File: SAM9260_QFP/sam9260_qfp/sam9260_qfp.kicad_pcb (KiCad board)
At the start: 4 copper layers, 164 parts, among them J101 Conn_ARM_JTAG_SWD_10, J201 USB_B_Micro, J202 Micro_SD_Card, J203 RJ45, J301 USB_A, J302 USB_A, SW101 SW_Push, SW102 SW_DIP_x01, U101 AT91SAM9260-QU, U201 USBLC6-2SC6, U202 LD1117S33TR_SOT223, U203 RTL8211EG-VB-CG, U301 USBLC6-2SC6, U302 USB2514B_Bi, U303 MIC2099-1YMT-TR, U304 MIC2099-1YMT-TR, U305 USBLC6-2SC6, U306 USBLC6-2SC6, Y101 18MHz, Y201 25Mhz, Y301 24MHz

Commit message: Completed component placing
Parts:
- added C135: 4.7u, Capacitor_SMD:C_0603_1608Metric, F.Cu at (128.0, 82.0)
- added C235: 100n, Capacitor_SMD:C_0402_1005Metric, F.Cu at (95.7, 57.8)
- added FB101: 120R, Inductor_SMD:L_0603_1608Metric, F.Cu at (127.2, 84.5)
- FB201, FB301, FB302, FB303: footprint Inductor_SMD:L_0805_2012Metric -> Inductor_SMD:L_0603_1608Metric
- U101: footprint My_First_PCB:PQFP208_ATM -> SAM9260:PQFP208_ATM
- U303, U304: footprint My_First_PCB:TMLF-6_MT_MCH -> MIC2099:TMLF-6_MT_MCH
- XMER201: footprint My_First_PCB:H5007NL_PUL -> H5007NL:H5007NL_PUL
- moved C319 231.2 mm to (85.8, 167.8), turned to 180 degrees
- moved C321 222.7 mm to (86.3, 169.5), turned to 180 degrees
- moved J302 221.9 mm to (86.8, 175.3)
- moved D301 215.0 mm to (91.3, 153.0)
- moved U305 211.5 mm to (107.1, 164.0), turned to -90 degrees
- moved C318 210.5 mm to (105.8, 167.8), turned to 180 degrees
- moved C315 208.9 mm to (90.3, 137.7), turned to -90 degrees
- moved C323 207.8 mm to (86.3, 171.0), turned to 180 degrees
- moved R309 207.2 mm to (93.8, 150.8), turned to -90 degrees
- moved C312 207.0 mm to (92.0, 132.7), turned to 180 degrees
- moved C309 206.5 mm to (88.8, 137.7), turned to -90 degrees
- moved C224 206.1 mm to (66.3, 56.0)
- moved C305 203.2 mm to (89.5, 129.7), turned to 180 degrees
- moved C222 203.1 mm to (66.3, 57.5)
- moved C219 203.0 mm to (66.3, 60.5)
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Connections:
- C112 pad 1: +3.3V -> +3.3VA
- C113 pad 1: +3.3V -> +3.3VA
- C220 pad 1: Net-(C220-Pad1) -> AVDD10
- C223 pad 1: Net-(C220-Pad1) -> AVDD10
- C227 pad 1: Net-(C220-Pad1) -> AVDD10
- C229 pad 1: Net-(C229-Pad1) -> AVDD10
- C230 pad 1: Net-(C229-Pad1) -> AVDD10
- C231 pad 1: Net-(C229-Pad1) -> AVDD10
- J101 pad 1: AVDD10 -> +3.3V
- U101 pad 160: +3.3V -> +3.3VA

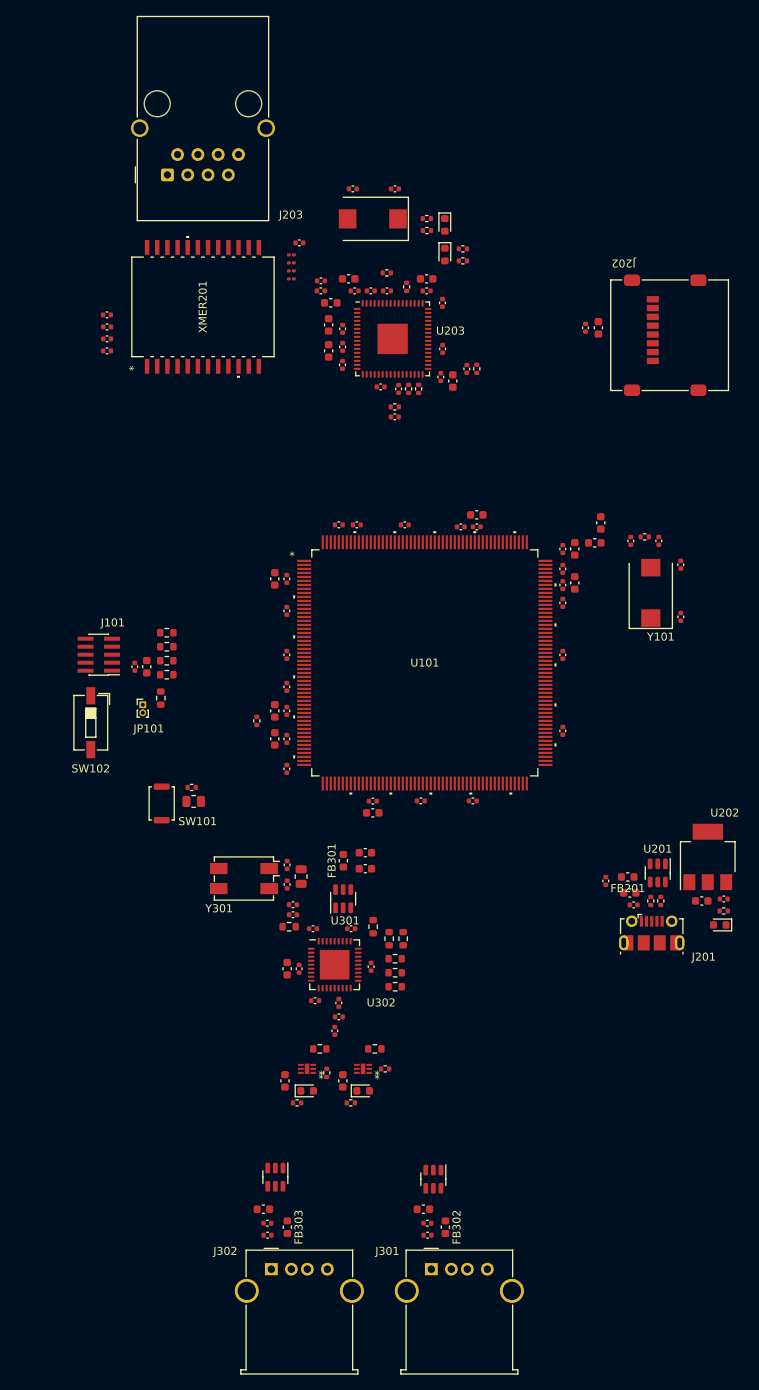
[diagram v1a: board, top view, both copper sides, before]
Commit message: updated layout
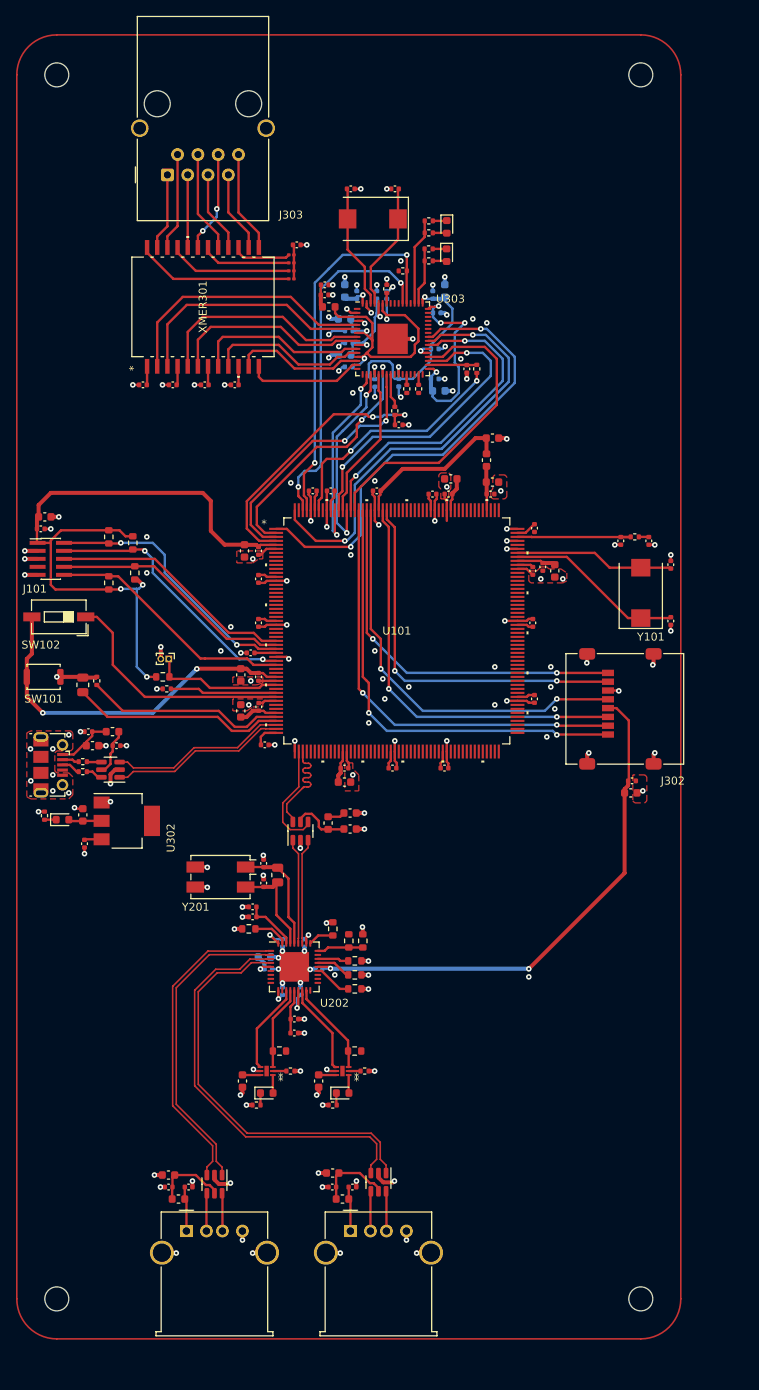
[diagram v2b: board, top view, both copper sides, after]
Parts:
- removed the C132 at (112.5, 81.0)
- removed the C135 at (128.0, 82.0)
- removed the R108 at (73.8, 97.5)
- removed the R109 at (73.8, 99.2)
- added C103: 10u, Capacitor_SMD:C_0603_1608Metric, F.Cu at (96.0, 114.4)
- added C111: 100n, Capacitor_SMD:C_0402_1005Metric, F.Cu at (119.5, 88.0)
- added H201: MountingHole, MountingHole:MountingHole_3mm, F.Cu at (133.0, 179.0)
- added H202: MountingHole, MountingHole:MountingHole_3mm, F.Cu at (60.0, 179.0)
- added H203: MountingHole, MountingHole:MountingHole_3mm, F.Cu at (60.0, 26.0)
- added H204: MountingHole, MountingHole:MountingHole_3mm, F.Cu at (133.0, 26.0)
- added R104: 1k, Resistor_SMD:R_0402_1005Metric, F.Cu at (65.0, 101.8)
- added R105: 100k, Resistor_SMD:R_0603_1608Metric, F.Cu at (69.8, 88.2)
- C102, C121, C123, C131: value 100n -> 10u; footprint Capacitor_SMD:C_0402_1005Metric -> Capacitor_SMD:C_0603_1608Metric
- C104, C110, C114, C122: value 10u -> 100n; footprint Capacitor_SMD:C_0603_1608Metric -> Capacitor_SMD:C_0402_1005Metric
- C113: value 4.7u -> 100n; footprint Capacitor_SMD:C_0603_1608Metric -> Capacitor_SMD:C_0402_1005Metric
- C120, C125: value 100n -> 4.7u; footprint Capacitor_SMD:C_0402_1005Metric -> Capacitor_SMD:C_0603_1608Metric
- C209: renamed from C309; moved to B.Cu
- C210: renamed from C310; moved to B.Cu
- C211: renamed from C311; moved to B.Cu
- C212: renamed from C312; moved to B.Cu
- C213: renamed from C313; moved to B.Cu
- C214: renamed from C314; moved to B.Cu
- C215: renamed from C315; moved to B.Cu
- C308: renamed from C208; moved to B.Cu
- C309: renamed from C209; moved to B.Cu
- C310: renamed from C210; moved to B.Cu
- C311: renamed from C211; moved to B.Cu
- C312: renamed from C212; moved to B.Cu
- C313: renamed from C213; moved to B.Cu
- C314: renamed from C214; moved to B.Cu
- C315: renamed from C215; moved to B.Cu
- C316: renamed from C216; moved to B.Cu
- C317: renamed from C217; moved to B.Cu
- C318: renamed from C220; moved to B.Cu
- C321: renamed from C223; moved to B.Cu
- C324: renamed from C227; moved to B.Cu
- C328: renamed from C235; moved to B.Cu
- C330: renamed from C229; moved to B.Cu
- C331: renamed from C230; moved to B.Cu
- C332: renamed from C231; moved to B.Cu
- R101: value 1.5M -> 1k; footprint Resistor_SMD:R_0805_2012Metric -> Resistor_SMD:R_0402_1005Metric
- R102: value 1k -> 1.5M; footprint Resistor_SMD:R_0402_1005Metric -> Resistor_SMD:R_0805_2012Metric
- R103: value 1k -> 100k; footprint Resistor_SMD:R_0402_1005Metric -> Resistor_SMD:R_0603_1608Metric
- U101: value AT91SAM9260-QU -> AT91SAM9260B-QU
- XMER301: renamed from XMER201; footprint H5007NL:H5007NL_PUL -> HL5007:H5007NL_PUL
- moved R303 85.7 mm to (58.5, 118.6), turned to -90 degrees
- moved D301 83.2 mm to (60.7, 119.1), turned to 0 degrees
- moved C304 80.2 mm to (63.5, 122.1), turned to -90 degrees
- moved C307 78.1 mm to (63.2, 118.5), turned to 90 degrees
- moved J301 78.0 mm to (59.2, 112.2), turned to -90 degrees
- moved R301 74.0 mm to (63.2, 113.1), turned to 0 degrees
- moved R302 73.1 mm to (63.2, 111.8), turned to 0 degrees
- moved U302 72.8 mm to (68.8, 119.2), turned to 0 degrees
- moved C302 71.5 mm to (63.9, 108.1)
- moved C301 69.6 mm to (64.5, 109.8), turned to 0 degrees
- moved U301 69.6 mm to (66.7, 112.8), turned to 180 degrees
- moved FB301 66.9 mm to (67.0, 108.1), turned to 0 degrees
- moved C128 66.8 mm to (58.5, 81.2), turned to 180 degrees
- moved C129 65.6 mm to (58.0, 82.8), turned to 180 degrees
- moved C303 63.5 mm to (67.5, 109.8), turned to 0 degrees
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- renumbered C103 to C132, C111 to C133, C133 to C134, C134 to C135, C301 to C201, C302 to C202, C303 to C203, C304 to C204, C305 to C205, C306 to C206, C307 to C207, C308 to C208, C316 to C216, C317 to C217, C318 to C218, C319 to C219, C320 to C220, C321 to C221, C322 to C222, C323 to C223, C201 to C301, C202 to C302, C203 to C303, C204 to C304, C205 to C305, C206 to C306, C207 to C307, C218 to C319, C219 to C320, C221 to C322, C222 to C323, C224 to C325, C225 to C326, C226 to C327, C228 to C329, C232 to C333, C233 to C334, C234 to C335, D301 to D201, D302 to D202, D201 to D301, D202 to D302, D203 to D303, FB301 to FB201, FB302 to FB202, FB303 to FB203, FB201 to FB301, J301 to J201, J302 to J202, J201 to J301, J202 to J302, J203 to J303, L201 to L301, R104 to R108, R105 to R109, R301 to R201, R302 to R202, R303 to R203, R304 to R204, R305 to R205, R306 to R206, R307 to R207, R308 to R208, R309 to R209, R310 to R210, R311 to R211, R312 to R212, R313 to R213, R314 to R214, R201 to R301, R202 to R302, R203 to R303, R204 to R304, R205 to R305, R206 to R306, R207 to R307, R208 to R308, R209 to R309, R210 to R310, R211 to R311, R212 to R312, R213 to R313, R214 to R314, R215 to R315, R216 to R316, R217 to R317, U301 to U201, U302 to U202, U303 to U203, U304 to U204, U305 to U205, U306 to U206, U201 to U301, U202 to U302, U203 to U303, Y301 to Y201, Y201 to Y301
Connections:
- net Net-(J101-SWO/TDO) renamed TD0_DBG
- net Net-(U101C-JTAGSEL) renamed JTAGSEL_DBG
- net Net-(U302-USBDM_DN1/PRT_DIS_M1) renamed /USB/USB_HUB1_N
- net Net-(U302-USBDM_DN2/PRT_DIS_M2) renamed /USB/USB_HUB2_N
- net Net-(U302-USBDM_UP) renamed /USB/USB_BOARD_N
- net Net-(U302-USBDP_DN1/PRT_DIS_P1) renamed /USB/USB_HUB1_P
- net Net-(U302-USBDP_DN2/PRT_DIS_P2) renamed /USB/USB_HUB2_P
- net Net-(U302-USBDP_UP) renamed /USB/USB_BOARD_P
- C101 pad 1: AVDD10 -> GND
- C101 pad 2: +3.3V -> VDD_IOM
- C102 pad 1: AVDD10 -> GND
- C102 pad 2: +3.3V -> VDD_CORE
- C104 pad 1: AVDD10 -> GND
- C104 pad 2: +1V8 -> VDD_IOM
- C105 pad 1: AVDD10 -> GND
- C105 pad 2: +1V8 -> VDD_CORE
- C106 pad 1: +3.3V -> VDD_IOM
- C106 pad 2: AVDD10 -> GND
- C107 pad 1: +3.3V -> GND
- C107 pad 2: AVDD10 -> VDD_IOM
- C108 pad 1: +3.3V -> GND
- C108 pad 2: AVDD10 -> VDD_CORE
- C109 pad 1: +3.3V -> VDD_IOM
- C109 pad 2: AVDD10 -> GND
- C110 pad 1: +3.3V -> GND
- C110 pad 2: AVDD10 -> VDD_IOM
- C112 pad 1: +3.3VA -> VDD_IOM
- C112 pad 2: AVDD10 -> GND
- C113 pad 1: +3.3VA -> GND
- C113 pad 2: AVDD10 -> VDD_IOM
- C114 pad 1: AVDD10 -> GND
- C114 pad 2: +3.3V -> VDD_CORE
- C115 pad 1: AVDD10 -> VDD_IOM
- C115 pad 2: +3.3V -> GND
- C116 pad 1: AVDD10 -> GND
- C116 pad 2: +3.3V -> VDD_IOM
- C117 pad 1: AVDD10 -> GND
- C117 pad 2: +3.3V -> VDD_CORE
- C118 pad 1: AVDD10 -> GND
- C118 pad 2: +3.3V -> VDD_IOM
- C119 pad 1: AVDD10 -> GND
- C119 pad 2: +3.3V -> VDD_IOM
- C120 pad 1: AVDD10 -> VDD_IOM
- C120 pad 2: +3.3V -> GND
- C121 pad 1: AVDD10 -> GND
- C121 pad 2: +3.3V -> VDD_CORE
- C122 pad 1: AVDD10 -> GND
- C122 pad 2: +1V8 -> VDD_CORE
- C123 pad 1: AVDD10 -> VDD_IOP1
- C123 pad 2: +1V8 -> GND
- C124 pad 1: AVDD10 -> GND
- C124 pad 2: +1V8 -> VDD_CORE
- C125 pad 1: AVDD10 -> VDD_ANA
- C125 pad 2: +1V8 -> GND
- C126 pad 1: AVDD10 -> VDD_IOP1
- C126 pad 2: +1V8 -> GND
- C127 pad 1: AVDD10 -> VDD_ANA
- C127 pad 2: +1V8 -> GND
- C128 pad 1: AVDD10 -> GND
- C128 pad 2: +1V8 -> VDD_IOM
- C129 pad 1: AVDD10 -> GND
- C129 pad 2: +1V8 -> VDD_IOM
- C130 pad 1: AVDD10 -> GND
- C130 pad 2: +1V8 -> VDD_CORE
- C131 pad 1: +2V5 -> GND
- C131 pad 2: AVDD10 -> VDD_CORE
- C132 pad 1: AVDD10 -> GND
- C133 pad 1: AVDD10 -> GND
- C134 pad 1: AVDD10 -> GND
- C135 pad 1: AVDD10 -> GND
- C201 pad 2: AVDD10 -> GND
- C202 pad 2: AVDD10 -> GND
- C203 pad 2: AVDD10 -> GND
- C204 pad 2: AVDD10 -> GND
- C205 pad 2: AVDD10 -> GND
- C206 pad 2: AVDD10 -> GND
- C207 pad 2: AVDD10 -> GND
- C208 pad 2: AVDD10 -> GND
- C209 pad 1: +3V3 -> AVDD33
- C209 pad 2: AVDD10 -> GND
- C210 pad 1: +3V3 -> AVDD33
- C210 pad 2: AVDD10 -> GND
- C211 pad 1: +3V3 -> AVDD33
- C211 pad 2: AVDD10 -> GND
- C212 pad 1: +3V3 -> AVDD33
- C212 pad 2: AVDD10 -> GND
- C213 pad 1: +3V3 -> AVDD33
- C213 pad 2: AVDD10 -> GND
- C214 pad 1: +3V3 -> AVDD33
- C214 pad 2: AVDD10 -> GND
- C215 pad 1: +3V3 -> AVDD33
- C215 pad 2: AVDD10 -> GND
- C216 pad 2: AVDD10 -> GND
- C217 pad 2: AVDD10 -> GND
- C218 pad 2: AVDD10 -> GND
- C219 pad 2: AVDD10 -> GND
- C220 pad 2: AVDD10 -> GND
- C221 pad 2: AVDD10 -> GND
- C222 pad 2: AVDD10 -> GND
- C223 pad 2: AVDD10 -> GND
- C301 pad 2: AVDD10 -> GND
- C302 pad 2: AVDD10 -> GND
- C303 pad 2: AVDD10 -> GND
- C304 pad 2: AVDD10 -> GND
- C305 pad 1: +3V3 -> AVDD33
- C305 pad 2: AVDD10 -> GND
- C306 pad 1: +3V3 -> AVDD33
- C306 pad 2: AVDD10 -> GND
- C307 pad 1: +3V3 -> AVDD33
- C307 pad 2: AVDD10 -> GND
- C308 pad 1: +3V3 -> AVDD33
- C308 pad 2: AVDD10 -> GND
- C309 pad 1: +3V3 -> AVDD33
- C309 pad 2: AVDD10 -> GND
- C310 pad 1: +3V3 -> AVDD33
- C310 pad 2: AVDD10 -> GND
- C311 pad 1: +3V3 -> AVDD33
- C311 pad 2: AVDD10 -> GND
- C312 pad 1: +3V3 -> AVDD33
- C312 pad 2: AVDD10 -> GND
- C313 pad 1: +3V3 -> AVDD33
- C313 pad 2: AVDD10 -> GND
- C314 pad 1: +3V3 -> AVDD33
- C314 pad 2: AVDD10 -> GND
- C315 pad 1: +3V3 -> AVDD33
- C315 pad 2: AVDD10 -> GND
- C316 pad 1: +3V3 -> AVDD33
- C316 pad 2: AVDD10 -> GND
- C317 pad 1: +3V3 -> AVDD33
- C317 pad 2: AVDD10 -> GND
- C318 pad 1: AVDD10 -> REG_OUT
- C318 pad 2: AVDD10 -> GND
- C319 pad 1: AVDD10 -> GND
- C320 pad 2: AVDD10 -> GND
- C321 pad 1: AVDD10 -> REG_OUT
- C321 pad 2: AVDD10 -> GND
- C322 pad 2: AVDD10 -> GND
- C323 pad 2: AVDD10 -> GND
- C324 pad 1: AVDD10 -> REG_OUT
- C324 pad 2: AVDD10 -> GND
- C325 pad 2: AVDD10 -> GND
- C326 pad 1: AVDD10 -> GND
- C327 pad 1: AVDD10 -> Net-(C327-Pad1)
- C327 pad 2: AVDD10 -> GND
- C328 pad 1: AVDD10 -> REG_OUT
- C328 pad 2: AVDD10 -> GND
- C329 pad 1: AVDD10 -> Net-(C327-Pad1)
- C329 pad 2: AVDD10 -> GND
- C330 pad 1: AVDD10 -> REG_OUT
- C330 pad 2: AVDD10 -> GND
- C331 pad 1: AVDD10 -> REG_OUT
- C331 pad 2: AVDD10 -> GND
- C332 pad 1: AVDD10 -> REG_OUT
- C332 pad 2: AVDD10 -> GND
- C333 pad 2: AVDD10 -> GND
- C334 pad 2: AVDD10 -> GND
- C335 pad 2: AVDD10 -> GND
- D301 pad 2: +3V3 -> AVDD33
- D302 pad 1: +3V3 -> AVDD33
- D303 pad 1: +3V3 -> AVDD33
- FB101 pad 1: +3.3V -> VDD_IOM
- FB101 pad 2: +3.3VA -> VDD_ANA
- J101 pad 1: +3.3V -> VDD_IOM
- J101 pad 10: Net-(J101-~{RESET}) -> NTRST_DBG
- J101 pad 2: Net-(J101-SWDIO/TMS) -> TMS_DBG
- J101 pad 3: AVDD10 -> GND
- J101 pad 4: Net-(J101-SWDCLK/TCK) -> TCK_DBG
- J101 pad 5: AVDD10 -> GND
- J101 pad 8: Net-(J101-NC/TDI) -> TD1_DBG
- J101 pad 9: AVDD10 -> GND
- J201 pad 4: AVDD10 -> GND
- J201 pad 5: AVDD10 -> GND
- J202 pad 4: AVDD10 -> GND
- J202 pad 5: AVDD10 -> GND
- J301 pad 5: AVDD10 -> GND
- J301 pad 6: AVDD10 -> GND
- J302 pad 4: AVDD10 -> AVDD33
- J302 pad 6: AVDD10 -> GND
- JP101 pad 2: AVDD10 -> GND
- L301 pad 2: AVDD10 -> Net-(C327-Pad1)
- R101 pad 1: +1V8 -> GND
- R101 pad 2: Net-(U101B-SHDN) -> Net-(U101A-TST)
- R102 pad 1: AVDD10 -> GND
- R102 pad 2: Net-(U101B-TST) -> Net-(U101A-SHDN)
- R103 pad 1: +1V8 -> VDD_IOM
- R103 pad 2: Net-(U101B-WKUP) -> NTRST_DBG
- R106 pad 1: +3.3V -> VDD_IOM
- R106 pad 2: Net-(J101-~{RESET}) -> TMS_DBG
- R107 pad 1: +3.3V -> VDD_IOM
- R107 pad 2: Net-(J101-NC/TDI) -> TCK_DBG
- R108 pad 2: +3.3V -> VDD_IOM
- R202 pad 2: AVDD10 -> GND
- R204 pad 1: AVDD10 -> GND
- R205 pad 1: AVDD10 -> GND
- R206 pad 1: AVDD10 -> GND
- R207 pad 1: AVDD10 -> GND
- R208 pad 1: AVDD10 -> GND
- R209 pad 2: AVDD10 -> GND
- R211 pad 2: AVDD10 -> GND
- R213 pad 2: AVDD10 -> GND
- R214 pad 2: AVDD10 -> GND
- R303 pad 1: AVDD10 -> GND
- R304 pad 2: +3V3 -> AVDD33
- R305 pad 2: +3V3 -> AVDD33
- R306 pad 2: AVDD10 -> AVDD33
- R307 pad 2: AVDD10 -> GND
- R310 pad 2: +3V3 -> AVDD33
- R317 pad 2: +3V3 -> AVDD33
- SW101 pad 1: AVDD10 -> VDD_CORE
- SW101 pad 2: +1V8 -> GND
- SW102 pad 2: +1V8 -> VDD_CORE
- U101 pad 113: AVDD10 -> GND
- U101 pad 114: +3.3V -> VDD_IOM
- U101 pad 13: +3.3V -> VDD_IOM
- U101 pad 132: +3.3V -> VDD_IOM
- U101 pad 133: AVDD10 -> GND
- U101 pad 14: AVDD10 -> GND
- U101 pad 146: AVDD10 -> GND
- U101 pad 147: +1V8 -> VDD_CORE
- U101 pad 148: +1V8 -> VDD_CORE
- U101 pad 151: AVDD10 -> GND
- U101 pad 153: AVDD10 -> GND
- U101 pad 155: +1V8 -> VDD_CORE
- U101 pad 156: AVDD10 -> GND
- U101 pad 160: +3.3VA -> VDD_ANA
- U101 pad 169: +2V5 -> VDD_IOP1
- U101 pad 170: AVDD10 -> GND
- U101 pad 173: AVDD10 -> GND
- U101 pad 174: +1V8 -> VDD_CORE
- U101 pad 187: +3.3V -> VDD_IOM
- U101 pad 188: AVDD10 -> GND
- U101 pad 199: +3.3V -> VDD_IOM
- U101 pad 200: AVDD10 -> GND
- U101 pad 202: GTX_CLK -> GTX_CLK_N
- U101 pad 203: +1V8 -> VDD_CORE
- U101 pad 204: AVDD10 -> GND
- U101 pad 24: +3.3V -> VDD_IOM
- U101 pad 25: AVDD10 -> GND
- U101 pad 30: Net-(J101-NC/TDI) -> TD1_DBG
- U101 pad 31: Net-(J101-SWDIO/TMS) -> TMS_DBG
- U101 pad 32: +3.3V -> VDD_IOM
- U101 pad 33: AVDD10 -> GND
- U101 pad 34: Net-(J101-SWDCLK/TCK) -> TCK_DBG
- U101 pad 35: Net-(J101-~{RESET}) -> NTRST_DBG
- U101 pad 38: +1V8 -> VDD_CORE
- U101 pad 39: AVDD10 -> GND
- U101 pad 4: RX_CLK -> RX_CLK_N
- U101 pad 42: Net-(U101B-TST) -> Net-(U101A-TST)
- U101 pad 44: AVDD10 -> GND
- U101 pad 47: +1V8 -> VDD_CORE
- U101 pad 48: Net-(U101B-WKUP) -> Net-(U101A-WKUP)
- U101 pad 49: Net-(U101B-SHDN) -> Net-(U101A-SHDN)
- U101 pad 5: +3.3V -> VDD_IOM
- U101 pad 52: +3.3V -> VDD_IOM
- U101 pad 53: AVDD10 -> GND
- U101 pad 6: AVDD10 -> GND
- U101 pad 65: +3.3V -> VDD_IOM
- U101 pad 66: AVDD10 -> GND
- U101 pad 77: +1V8 -> VDD_CORE
- U101 pad 78: AVDD10 -> GND
- U101 pad 90: +3.3V -> VDD_IOM
- U101 pad 91: AVDD10 -> GND
- U201 pad 2: AVDD10 -> GND
- U202 pad 10: +3V3 -> AVDD33
- U202 pad 11: AVDD10 -> GND
- U202 pad 15: +3V3 -> AVDD33
- U202 pad 23: +3V3 -> AVDD33
- U202 pad 26: +3V3 -> AVDD33
- U202 pad 29: +3V3 -> AVDD33
- U202 pad 36: +3V3 -> AVDD33
- U202 pad 37: AVDD10 -> GND
- U202 pad 5: +3V3 -> AVDD33
- U203 pad 5: AVDD10 -> GND
- U203 pad 7: AVDD10 -> unconnected-(U203-Pad7)
- U204 pad 5: AVDD10 -> GND
- U204 pad 7: AVDD10 -> unconnected-(U204-Pad7)
- U205 pad 2: AVDD10 -> GND
- U206 pad 2: AVDD10 -> GND
- U301 pad 2: AVDD10 -> GND
- U302 pad 1: AVDD10 -> GND
- U302 pad 2: +3V3 -> AVDD33
- U303 pad 10: AVDD10 -> AVDD33
- U303 pad 13: AVDD10 -> REG_OUT
- U303 pad 2: AVDD10 -> GND
- U303 pad 20: AVDD10 -> AVDD33
- U303 pad 26: AVDD10 -> AVDD33
- U303 pad 33: AVDD10 -> REG_OUT
- U303 pad 37: AVDD10 -> AVDD33
- U303 pad 4: AVDD10 -> GND
- U303 pad 48: AVDD10 -> REG_OUT
- U303 pad 49: AVDD10 -> AVDD33
- U303 pad 57: +3V3 -> AVDD33
- U303 pad 59: AVDD10 -> REG_OUT
- U303 pad 60: AVDD10 -> AVDD33
- U303 pad 63: AVDD10 -> GND
- U303 pad 64: AVDD10 -> AVDD33
- U303 pad 65: AVDD10 -> GND
- U303 pad 7: AVDD10 -> REG_OUT
- Y201 pad 2: AVDD10 -> GND
- Y201 pad 3: AVDD10 -> GND
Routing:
- net GND: track 0.00 -> 174.2 mm, vias 0 -> 157
- net AVDD33: track 0.00 -> 140.0 mm, vias 0 -> 14
- net VDD_IOM: track 0.00 -> 128.5 mm, vias 0 -> 3
- net VDD_CORE: track 0.00 -> 65.6 mm, vias 0 -> 2
- net REG_OUT: track 0.00 -> 64.5 mm, vias 0 -> 7
- net TX_D3: track 0.00 -> 58.9 mm, vias 0 -> 2
- net SD_DAT2: track 0.00 -> 56.7 mm, vias 0 -> 2
- net +5V: track 0.00 -> 56.2 mm
- net SD_DAT3: track 0.00 -> 55.4 mm, vias 0 -> 2
- net TX_D2: track 0.00 -> 55.4 mm, vias 0 -> 2
- net /USB/USB_HUB2_N: track 0.00 -> 52.8 mm
- net /USB/USB_HUB2_P: track 0.00 -> 52.0 mm
- net SD_CLK: track 0.00 -> 51.6 mm, vias 0 -> 2
- net SD_CMD: track 0.00 -> 51.5 mm, vias 0 -> 2
- net MDC: track 0.00 -> 48.2 mm, vias 0 -> 2
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- added copper zone on F.Cu, net GND
- added copper zone on In1.Cu, net GND
- added copper zone on In2.Cu, net GND

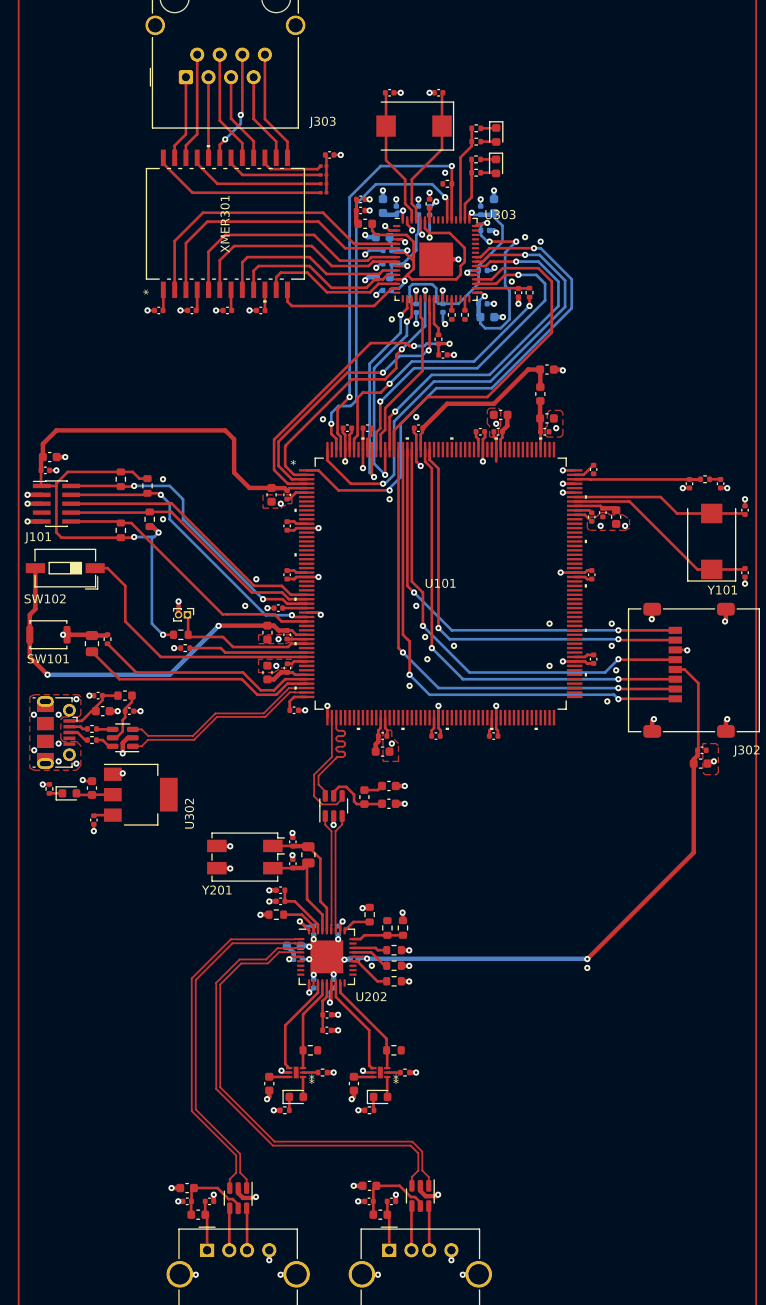
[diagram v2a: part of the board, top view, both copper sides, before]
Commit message: Completed routing, need to add logo
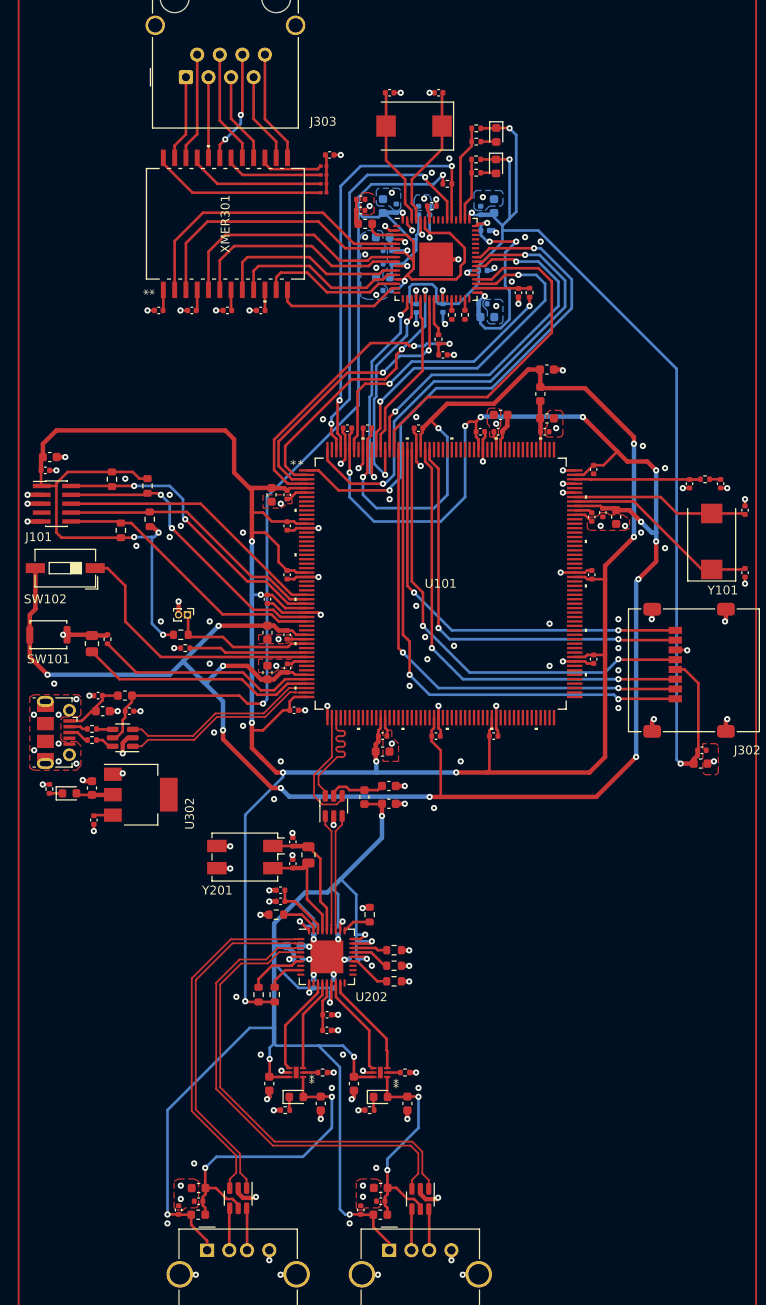
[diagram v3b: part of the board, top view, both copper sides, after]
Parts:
- removed R210, R212: DNP_12k, Resistor_SMD:R_0603_1608Metric
- removed R213, R214: 330R, Resistor_SMD:R_0402_1005Metric
- added C224: 2u2, Capacitor_SMD:C_0603_1608Metric, F.Cu at (89.0, 154.0)
- added C225: 2u2, Capacitor_SMD:C_0603_1608Metric, F.Cu at (98.8, 154.0)
- added R215: 10k, Resistor_SMD:R_0603_1608Metric, F.Cu at (82.0, 141.8)
- added R216: 10k, Resistor_SMD:R_0603_1608Metric, F.Cu at (83.8, 141.8)
- R201, R202: value 100k -> 330R; footprint Resistor_SMD:R_0603_1608Metric -> Resistor_SMD:R_0402_1005Metric
- XMER301: footprint HL5007:H5007NL_PUL -> H5007NL:H5007NL_PUL
- moved R201 23.5 mm to (85.0, 154.8), turned to 0 degrees
- moved R202 20.8 mm to (94.5, 154.8), turned to 0 degrees
- moved C223 3.59 mm to (93.5, 166.0), turned to 90 degrees
- moved C113 1.59 mm to (83.0, 97.2), turned to 90 degrees
- moved C222 1.38 mm to (73.0, 166.0), turned to 90 degrees
- moved C221 1.31 mm to (95.8, 165.0)
- moved C218 1.29 mm to (75.2, 163.5)
- moved C219 1.29 mm to (95.8, 163.5)
- moved C220 1.23 mm to (75.2, 165.0), turned to 180 degrees
- moved R106 1.00 mm to (65.5, 83.8)
- moved R307 0.35 mm to (101.5, 53.0), turned to 0 degrees
- moved U206 0.34 mm to (100.2, 164.8)
- moved C309 0.25 mm to (97.5, 53.2)
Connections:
- C101 pad 2: VDD_IOM -> AVDD33
- C103 pad 1: VDD_IOM -> AVDD33
- C104 pad 2: VDD_IOM -> AVDD33
- C106 pad 1: VDD_IOM -> AVDD33
- C107 pad 2: VDD_IOM -> AVDD33
- C109 pad 1: VDD_IOM -> AVDD33
- C110 pad 2: VDD_IOM -> AVDD33
- C112 pad 1: VDD_IOM -> AVDD33
- C113 pad 2: VDD_IOM -> AVDD33
- C115 pad 1: VDD_IOM -> AVDD33
- C116 pad 2: VDD_IOM -> AVDD33
- C118 pad 2: VDD_IOM -> AVDD33
- C119 pad 2: VDD_IOM -> AVDD33
- C120 pad 1: VDD_IOM -> AVDD33
- C128 pad 2: VDD_IOM -> AVDD33
- C129 pad 2: VDD_IOM -> AVDD33
- C202 pad 1: +5V -> VDD_IOPO
- C203 pad 1: +5V -> Net-(U201-VBUS)
- C209 pad 1: AVDD33 -> VDD_IOPO
- C210 pad 1: AVDD33 -> VDD_IOPO
- C211 pad 1: AVDD33 -> VDD_IOPO
- C212 pad 1: AVDD33 -> VDD_IOPO
- C213 pad 1: AVDD33 -> VDD_IOPO
- C214 pad 1: AVDD33 -> VDD_IOPO
- C215 pad 1: AVDD33 -> VDD_IOPO
- C216 pad 1: +5V -> VDD_IOPO
- C217 pad 1: +5V -> VDD_IOPO
- C218 pad 1: +5V -> 3V3_PORT1
- C219 pad 1: +5V -> 3V3_PORT2
- C220 pad 1: +5V -> 3V3_PORT1
- C221 pad 1: +5V -> 3V3_PORT2
- C222 pad 1: +5V -> VDD_IOPO
- C223 pad 1: +5V -> VDD_IOPO
- C303 pad 1: +5V -> AVDD33
- C304 pad 1: +5V -> AVDD33
- D201 pad 1: +5V -> Net-(D201-K)
- D201 pad 2: Net-(D201-A) -> 3V3_PORT1
- D202 pad 1: +5V -> Net-(D202-K)
- D202 pad 2: Net-(D202-A) -> 3V3_PORT2
- FB101 pad 1: VDD_IOM -> AVDD33
- FB201 pad 1: +5V -> VDD_IOPO
- FB201 pad 2: +5V -> Net-(U201-VBUS)
- FB202 pad 1: +5V -> 3V3_PORT1
- FB202 pad 2: +5V -> VDD_IOPO
- FB203 pad 1: +5V -> 3V3_PORT2
- FB203 pad 2: +5V -> VDD_IOPO
- FB301 pad 2: +5V -> AVDD33
- J101 pad 1: VDD_IOM -> AVDD33
- J201 pad 1: +5V -> VDD_IOPO
- J202 pad 1: +5V -> VDD_IOPO
- J302 pad 9: unconnected-(J302-SHIELD-Pad9) -> GND
- R103 pad 1: VDD_IOM -> AVDD33
- R105 pad 1: VDD_IOM -> AVDD33
- R106 pad 1: VDD_IOM -> AVDD33
- R107 pad 1: VDD_IOM -> AVDD33
- R108 pad 2: VDD_IOM -> AVDD33
- R201 pad 1: +5V -> GND
- R201 pad 2: /USB/VBUS_DET -> Net-(D201-K)
- R202 pad 1: /USB/VBUS_DET -> GND
- R202 pad 2: GND -> Net-(D202-K)
- U101 pad 114: VDD_IOM -> AVDD33
- U101 pad 13: VDD_IOM -> AVDD33
- U101 pad 132: VDD_IOM -> AVDD33
- U101 pad 187: VDD_IOM -> AVDD33
- U101 pad 199: VDD_IOM -> AVDD33
- U101 pad 24: VDD_IOM -> AVDD33
- U101 pad 32: VDD_IOM -> AVDD33
- U101 pad 5: VDD_IOM -> AVDD33
- U101 pad 52: VDD_IOM -> AVDD33
- U101 pad 65: VDD_IOM -> AVDD33
- U101 pad 90: VDD_IOM -> AVDD33
- U201 pad 5: +5V -> Net-(U201-VBUS)
- U202 pad 10: AVDD33 -> VDD_IOPO
- U202 pad 15: AVDD33 -> VDD_IOPO
- U202 pad 23: AVDD33 -> VDD_IOPO
- U202 pad 26: AVDD33 -> VDD_IOPO
- U202 pad 27: /USB/VBUS_DET -> VDD_IOPO
- U202 pad 29: AVDD33 -> VDD_IOPO
- U202 pad 36: AVDD33 -> VDD_IOPO
- U202 pad 5: AVDD33 -> VDD_IOPO
- U202 pad 6: unconnected-(U202-USBDM_DN3/PRT_DIS_M3-Pad6) -> Net-(U202-USBDM_DN3/PRT_DIS_M3)
- U202 pad 8: unconnected-(U202-USBDM_DN4/PRT_DIS_M4-Pad8) -> Net-(U202-USBDM_DN4/PRT_DIS_M4)
- U203 pad 1: Net-(D201-A) -> 3V3_PORT1
- U203 pad 6: +5V -> VDD_IOPO
- U204 pad 1: Net-(D202-A) -> 3V3_PORT2
- U204 pad 6: +5V -> VDD_IOPO
- U205 pad 5: +5V -> 3V3_PORT1
- U206 pad 5: +5V -> 3V3_PORT2
- U301 pad 5: +5V -> AVDD33
- U302 pad 3: +5V -> AVDD33
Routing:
- net AVDD33: track 140.0 -> 603.5 mm, vias 14 -> 26
- net VDD_CORE: track 65.6 -> 240.0 mm, vias 2 -> 15
- net VDD_IOPO: track 0.00 -> 170.7 mm, vias 0 -> 13
- net VDD_IOM: track 128.5 -> 0.00 mm, vias 3 -> 0
- net +5V: track 56.2 -> 0.00 mm
- net 3V3_PORT1: track 0.00 -> 35.5 mm, vias 0 -> 2
- net 3V3_PORT2: track 0.00 -> 25.7 mm, vias 0 -> 2
- net GND: track 174.2 -> 164.5 mm, vias 157 -> 180
- net Net-(U202-USBDM_DN3/PRT_DIS_M3): track 0.00 -> 6.50 mm
- net Net-(U201-VBUS): track 0.00 -> 6.02 mm
- net /USB/VBUS_DET: track 5.80 -> 0.00 mm
- net unconnected-(J302-SHIELD-Pad9): track 5.46 -> 0.00 mm, vias 4 -> 0
- net Net-(U202-USBDM_DN4/PRT_DIS_M4): track 0.00 -> 4.16 mm
- net Net-(D202-A): track 2.27 -> 0.00 mm
- net Net-(D201-A): track 2.26 -> 0.00 mm
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- added copper zone on B.Cu, net GND

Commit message: Added logo
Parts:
- added G***: LOGO, LOGO, F.Cu at (122.2, 163.2)
- moved J301 1.00 mm to (58.2, 112.2)
- turned D302 to 90 degrees
- turned D303 to 90 degrees
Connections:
- D302 pad 1: AVDD33 -> Net-(D302-K)
- D302 pad 2: Net-(D302-A) -> AVDD33
- D303 pad 1: AVDD33 -> Net-(D303-K)
- D303 pad 2: Net-(D303-A) -> AVDD33
- R308 pad 2: Net-(D302-A) -> Net-(D302-K)
- R315 pad 2: Net-(D303-A) -> Net-(D303-K)
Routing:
- net Net-(D302-K): track 0.00 -> 1.76 mm
- net Net-(D302-A): track 1.76 -> 0.00 mm
- net Net-(D303-K): track 0.00 -> 1.70 mm
- net Net-(D303-A): track 1.70 -> 0.00 mm
- net Net-(J301-VBUS): track 7.24 -> 8.24 mm
- net Net-(J301-D-): track 2.13 -> 3.13 mm
- net Net-(J301-D+): track 2.38 -> 3.38 mm
